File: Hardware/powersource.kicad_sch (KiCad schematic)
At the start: 34 parts, among them J10 USB_C_Receptacle_USB2.0_16P, J14 Conn_01x01_Socket, J15 Conn_01x01_Socket, J6 Conn_01x01_Socket, J9 Conn_01x01_Socket, Q2 DMP3015LSS-13, SW1 SW_Push_DPDT, U4 TPS61022, U8 CN3158

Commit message: S31 fully connected
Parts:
- added D13, D14: BSDFN2C031U, PCM_JLCPCB:D_DFN1006-2L, symbol YV-library:TVS-BSDFN2C031U
- added F1, F2, F3: BSMD1812-300-16V, Fuse:Fuse_1812_4532Metric_Pad1.30x3.40mm_HandSolder, symbol YV-library:Fuse-BSMD1812-300-16V
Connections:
- net GND: now also D13.1 (A1), D14.1 (A1)
- net USB-Dn: now also D14.2 (A2)
- net USB-Dp: now also D13.2 (A2)
- net V-USB: now also F3.2; no longer J10.A4 (VBUS), J10.A9 (VBUS), J10.B4 (VBUS), J10.B9 (VBUS)
- net Vbatt: now also F1.1, F2.1; no longer J14.1 (Pin_1), J6.1 (Pin_1)
- new net: F3.1, J10.A4 (VBUS), J10.A9 (VBUS), J10.B4 (VBUS), J10.B9 (VBUS)
- new net: F1.2, J14.1 (Pin_1)
- new net: F2.2, J6.1 (Pin_1)
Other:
- note removed: "Fuse"

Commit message: Schematic Done
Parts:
- removed C33: 4.7nF, Capacitor_SMD:C_0402_1005Metric, symbol Device:C
- removed JP1, JP2: SolderJumper_2_Bridged, Jumper:SolderJumper-2_P1.3mm_Bridged_Pad1.0x1.5mm, symbol Jumper:SolderJumper_2_Bridged
- removed JP3: SolderJumper_2_Open, Jumper:SolderJumper-2_P1.3mm_Open_TrianglePad1.0x1.5mm, symbol Jumper:SolderJumper_2_Open
- removed R36, R37: 732k, Resistor_SMD:R_0402_1005Metric, symbol Device:R
- removed R5: 180, Resistor_SMD:R_0402_1005Metric, symbol Device:R
- added C7, C8: 470nF, Capacitor_SMD:C_0402_1005Metric, symbol YV-library:CAPX470NM16V0-00
- added NT1: NetTie_2, NetTie:NetTie-2_SMD_Pad0.5mm, symbol Device:NetTie_2
- added R12: 357Ω, Resistor_SMD:R_0603_1608Metric, symbol YV-library:RES357RM-00
- added R9: 10mΩ, Resistor_SMD:R_1206_3216Metric, symbol YV-library:RESR010M-00
- added U3: MAX17055ETB+T, YV:TDFN-10-EP-2x2p5-0p4mm, symbol YV-library:MAX17055
- renumbered J6 to J1, J14 to J2, J9 to J7, J15 to J8
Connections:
- net GND: now also R9.2, U3.5 (CSn); no longer J7.1 (Pin_1), J8.1 (Pin_1)
- net V-USB: now also R12.1
- net Vbatt: now also C8.2, U3.10 (BATT)
- net at D7.2 (A), D8.2 (A): now also R12.2
- new net: NT1.2, U3.6 (CSp)
- new net: C7.2, U3.7 (REG)
- new net GNDREF: C7.1, C8.1, J7.1 (Pin_1), J8.1 (Pin_1), NT1.1, R9.1, U3.11 (EP), U3.2 (AIN)
- new net I2C-SCL: U3.3 (SCL)
- new net I2C-SDA: U3.4 (SDA)
- no-connect marks 6 -> 8
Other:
- note added: "2x18650 cell 3.2V LiFePO4 1500 mAh"
- note added: "BATT or USB to 5V"
- note added: "LiFePO4 BATTERIES Cell Fuel Gauge"
- note removed: "2x18650 cell 3.2V LiFePO4"
- note removed: "BATT / USB TO 5V"
- note removed: "Cell Gauge"
- note removed: "LiFePO4 BATTERIES"
- note removed: "LiFePo4 BATTERIES MONITORING (allow to choose ESP'S VN instead)"
- company: (none) -> Motion Composites
- title: (none) -> Strain Gauge Data Logger
- moved on the sheet: C1, C14, C25, C26, C27, D13, D14, D6, D7, D8, F1, F2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

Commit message: Layout: unrouted = 0
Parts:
- NT1: footprint NetTie:NetTie-2_SMD_Pad0.5mm -> YV:NetTie-2_SMD_Pad0.16mm
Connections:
- net USB-Dn: no longer D14.2 (A2)
- net USB-Dp: no longer D13.2 (A2)
- net at J10.A6 (D+), J10.B6 (D+), R7.1: now also D13.2 (A2)
- net at J10.A7 (D-), J10.B7 (D-), R6.1: now also D14.2 (A2)
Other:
- moved on the sheet: D13, D14

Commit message: Layout cleaned
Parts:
- renumbered C14 to C10, C1 to C11, C25 to C12, C8 to C31, C7 to C32, C27 to C8, C26 to C9, D14 to D12, D7 to D14, D8 to D15, D6 to D9, F2 to F1, F1 to F2, J10 to J6, L8 to L4, Q2 to Q1, R32 to R10, R12 to R11, R35 to R14, R9 to R24, R31 to R29, R6 to R31, R7 to R32, R16 to R33, R34 to R7, R33 to R8, R4 to R9, U4 to U2, U8 to U5, U3 to U8
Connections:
- net D-: now reaches D12.2 (A2), J6.A7 (D-), J6.B7 (D-), R31.1
- net D+: now reaches D13.2 (A2), J6.A6 (D+), J6.B6 (D+), R32.1
- net USB-Dn renamed USB_D-
- net USB-Dp renamed USB_D+

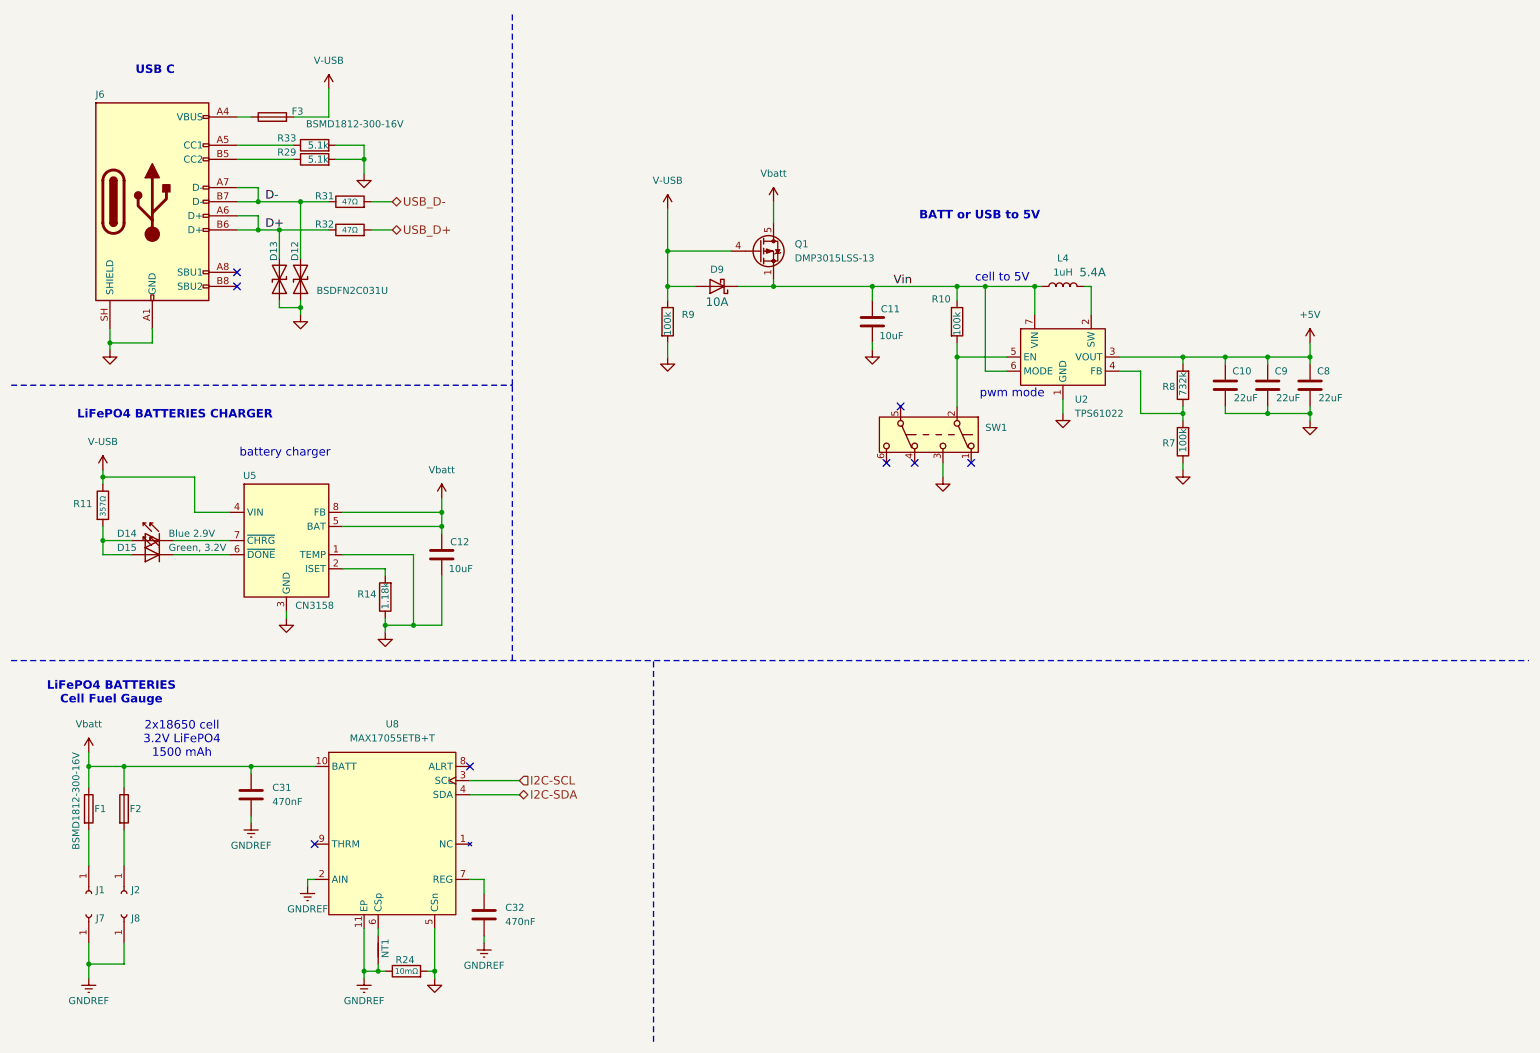
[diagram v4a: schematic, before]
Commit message: Update de la librairy et du BOM
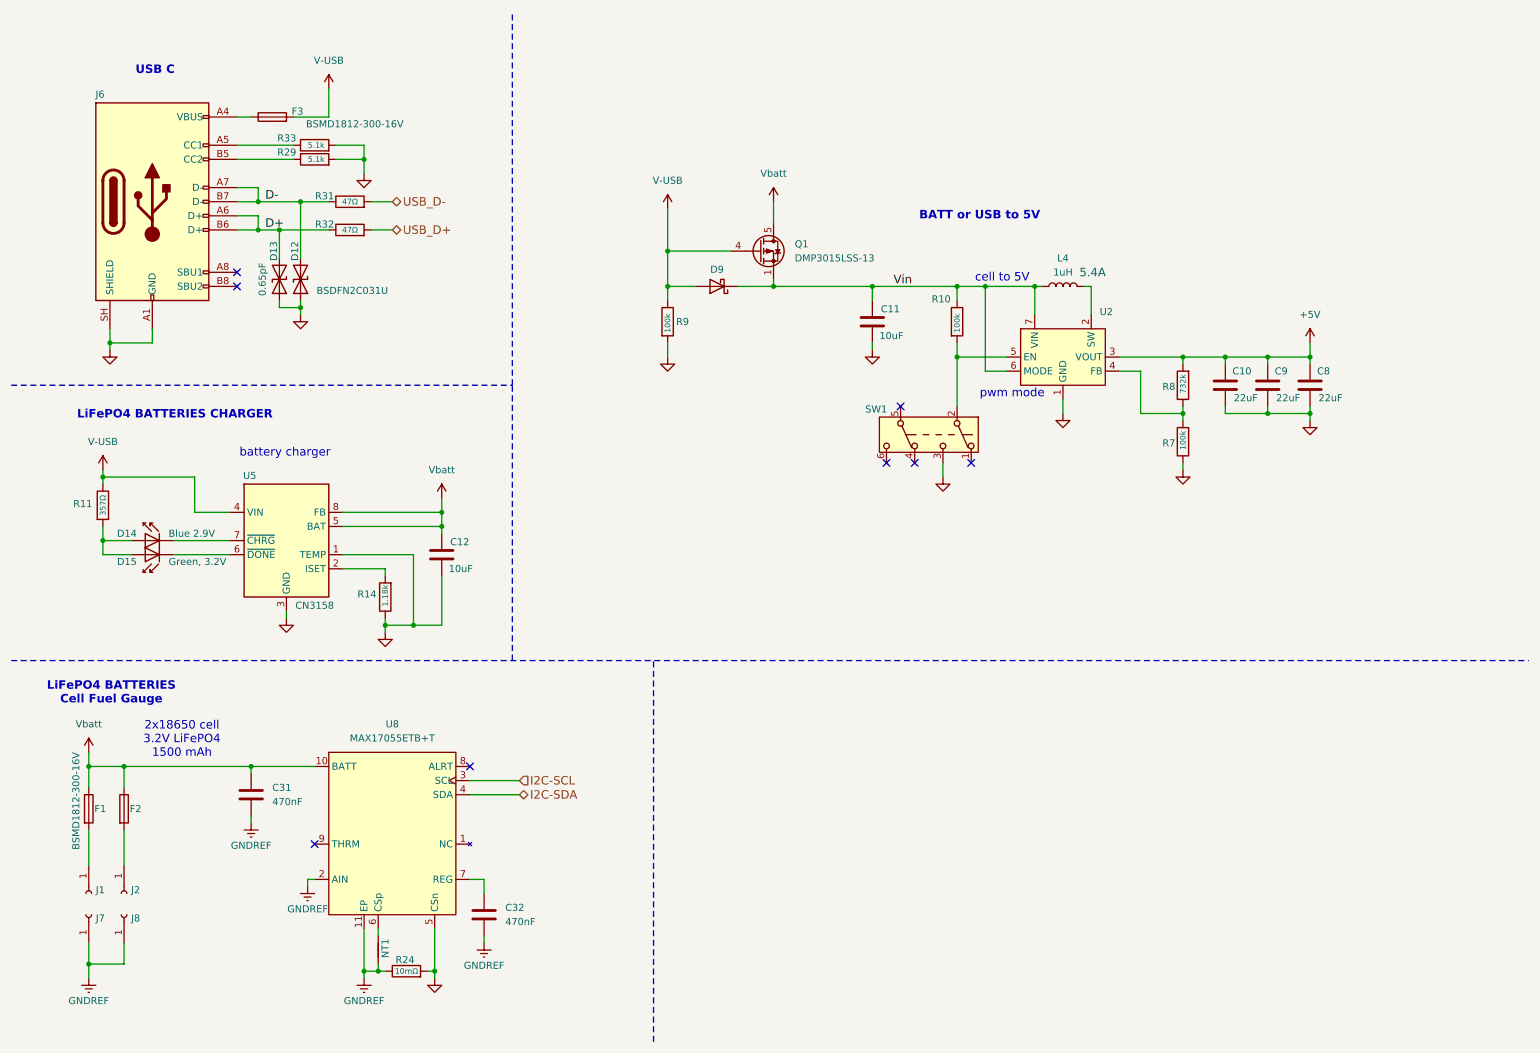
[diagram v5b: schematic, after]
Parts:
- C10, C8, C9: symbol Device:C -> YV-library:CAPX20U0P10V0-00
- C11, C12: symbol Device:C -> YV-library:CAPX10U0M6V30-00; LCSC C20069813 -> C15525; PartNumber CSA0402X7R474K100GT -> CL05A106MQ5NUNC
- D12, D13: Capacitance (none) -> 0.65pF
- D14: symbol LED:CQY99 -> YV-library:LEDN2V90-Blue-00; ParNumber GL0603UB01 -> (none); PartNumber (none) -> GL0603UB01
- D15: symbol LED:CQY99 -> YV-library:LEDN3V20-EGreen-00; ParNumber GL0603UG01 -> (none); PartNumber (none) -> GL0603UG01
- D9: value Fuxinsemi_PDS760 -> Diode-PDS760; symbol Diode:Fuxinsemi_PDS760 -> YV-library:Diode-PDS760; Current 10A -> (none); PartNumber (none) -> PDS760
- F1, F2, F3: PartNumber (none) -> BSMD1812-300-16V
- J6: value USB_C_Receptacle_USB2.0_16P -> USB_C_Receptacle-16p; symbol Connector:USB_C_Receptacle_USB2.0_16P -> YV-library:USB_C_Receptacle-16p; LSCS C3025063 -> (none); PartNumber (none) -> USB4105-GF-A-060
- L4: symbol Device:L -> YV-library:IND-XAL5030
- NT1: footprint YV:NetTie-2_SMD_Pad0.16mm -> (none)
- Q1: symbol Transistor_FET:IRF7606PBF -> YV-library:Mosfet-IRF7606PBF
- R10, R9: symbol Device:R -> YV-library:RES100KM-00; KiLib_Generator SMD_2terminal_chip_molded -> (none); PartNumber (none) -> 0402WGF1003TCE
- R11: footprint Resistor_SMD:R_0603_1608Metric -> Resistor_SMD:R_0402_1005Metric; LCSC C4288428 -> C852736; PartNumber TNPW0603357RBEEA -> RT0402BRD07357RL
- R14: symbol Device:R -> YV-library:RES1K18M-00
- R24: symbol YV-library:RESR010M-00 -> YV-library:RESR010P-00
- R29, R33: symbol Device:R -> YV-library:RES5K10M-00; PartNumber (none) -> SC0402J5101F2ANRH
- R7: symbol Device:R -> YV-library:RES100KM-00; LCSC C2909355 -> C25741; PartNumber (none) -> 0402WGF1003TCE
- R8: symbol Device:R -> YV-library:RES732KM-00; PartNumber (none) -> 0402WGF7323TCE
- SW1: symbol Switch:SW_Push_DPDT -> YV-library:SW_Push_DPDT; now in the parts list
- U2: value TPS61022 -> IC-TPS61022; symbol Converter_DCDC:TPS61022 -> YV-library:IC-TPS61022; PartNumber (none) -> TPS61022RWUR
- U5: symbol Battery_Management:CN3158 -> YV-library:CN3158; PartNumber (none) -> CN3158
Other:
- moved on the sheet: D15
